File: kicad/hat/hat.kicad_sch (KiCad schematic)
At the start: 6 parts, among them J1 GPIO, J2 FrontButtons, J3 DisplaySPI, J4 DisplayOnOff, J5 PowerButton, J6 PowerWakeup

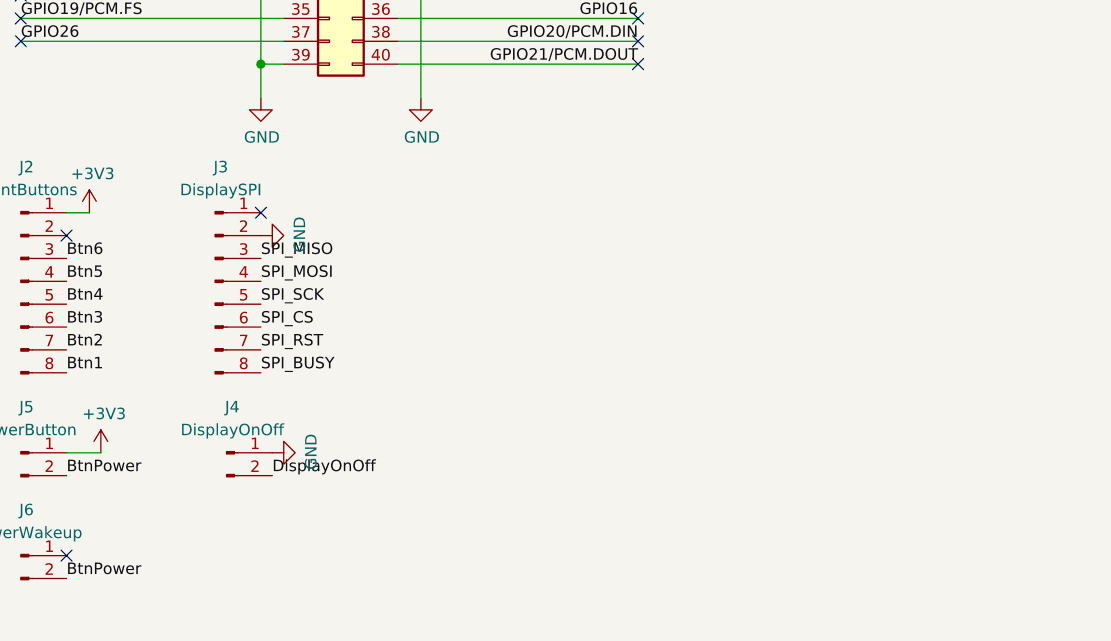
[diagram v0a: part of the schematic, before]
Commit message: addd display on off switch to hat
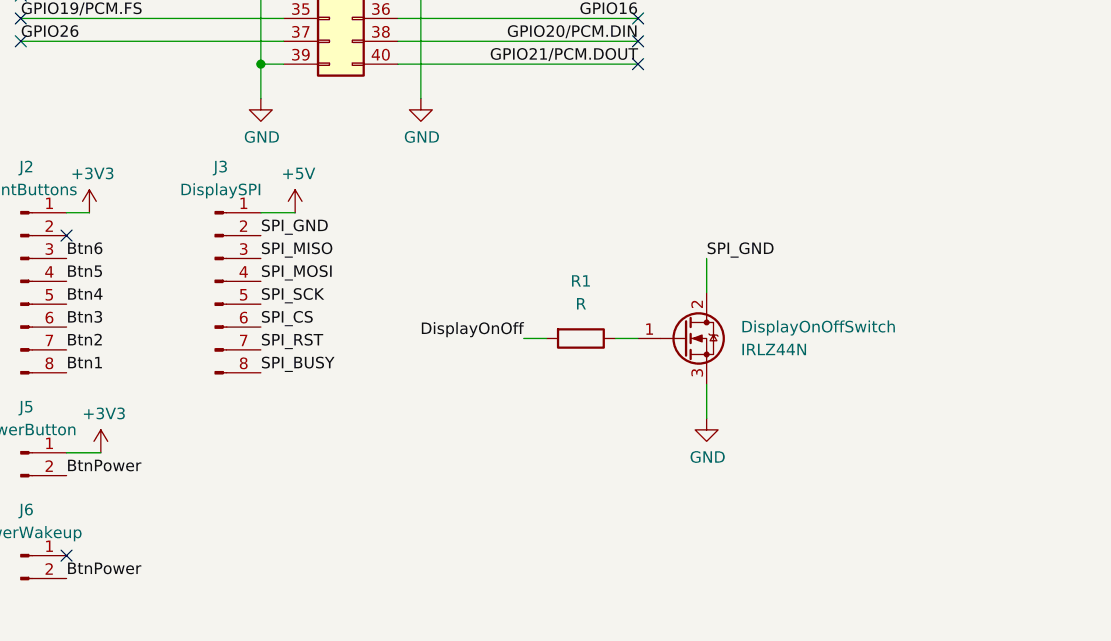
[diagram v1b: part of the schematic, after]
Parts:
- removed J4: DisplayOnOff, symbol Connector:Conn_01x02_Pin
- added DisplayOnOffSwitch: IRLZ44N, Package_TO_SOT_THT:TO-220-3_Vertical, symbol Transistor_FET:IRLZ44N
- added R1: R, symbol Device:R
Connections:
- net +5V: now also J3.1 (Pin_1)
- net DisplayOnOff: now also R1.2
- net GND: now also DisplayOnOffSwitch.3 (S); no longer J3.2 (Pin_2)
- new net: DisplayOnOffSwitch.1 (G), R1.1
- new net SPI_GND: DisplayOnOffSwitch.2 (D), J3.2 (Pin_2)
- no-connect marks 17 -> 16

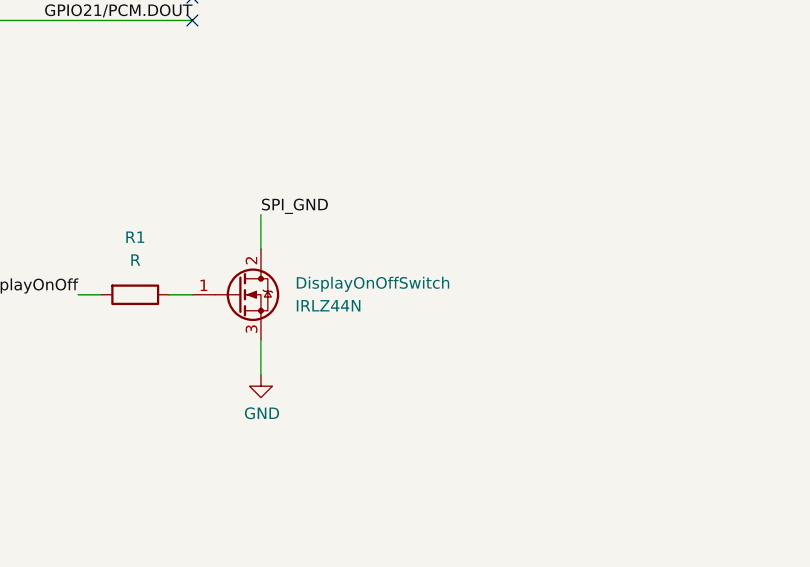
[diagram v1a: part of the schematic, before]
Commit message: add footprints to hat
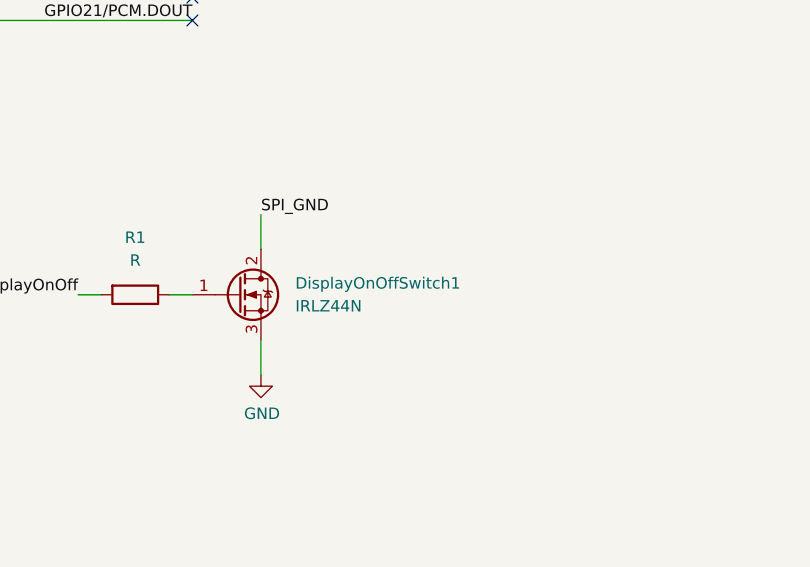
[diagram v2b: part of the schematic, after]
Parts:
- J2, J3: footprint (none) -> Connector_PinHeader_2.54mm:PinHeader_1x08_P2.54mm_Vertical
- J5, J6: footprint (none) -> Connector_PinHeader_2.54mm:PinHeader_1x02_P2.54mm_Vertical
- R1: footprint (none) -> Resistor_THT:R_Axial_DIN0207_L6.3mm_D2.5mm_P10.16mm_Horizontal
- renumbered DisplayOnOffSwitch to DisplayOnOffSwitch1
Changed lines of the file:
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@@
 			)
 		)
-		(property "Footprint" ""
+		(property "Footprint" "Resistor_THT:R_Axial_DIN0207_L6.3mm_D2.5mm_P10.16mm_Horizontal"
 			(at 105.41 111.252 90)
 			(hide yes)
@@
 			)
 		)
-		(property "Footprint" ""
+		(property "Footprint" "Connector_PinHeader_2.54mm:PinHeader_1x02_P2.54mm_Vertical"
 			(at 43.18 125.73 0)
 			(hide yes)
@@
 			)
 		)
-		(property "Footprint" ""
+		(property "Footprint" "Connector_PinHeader_2.54mm:PinHeader_1x02_P2.54mm_Vertical"
 			(at 43.18 137.16 0)
 			(hide yes)
@@
 		(dnp no)
 		(fields_autoplaced yes)
-		(property "Reference" "DisplayOnOffSwitch"
+		(property "Reference" "DisplayOnOffSwitch1"
 			(at 123.19 111.7599 0)
 			(show_name no)
@@
 			(project "hat"
 				(path "/e63e39d7-6ac0-4ffd-8aa3-1841a4541b55"
-					(reference "DisplayOnOffSwitch")
+					(reference "DisplayOnOffSwitch1")
 					(unit 1)
 				)
@@
 			)
 		)
-		(property "Footprint" ""
+		(property "Footprint" "Connector_PinHeader_2.54mm:PinHeader_1x08_P2.54mm_Vertical"
 			(at 64.77 106.68 0)
 			(hide yes)
@@
 			)
 		)
-		(property "Footprint" ""
+		(property "Footprint" "Connector_PinHeader_2.54mm:PinHeader_1x08_P2.54mm_Vertical"
 			(at 43.18 106.68 0)
 			(hide yes)

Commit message: start buttons board
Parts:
- added J7: BatteryLevel, Connector_PinHeader_2.54mm:PinHeader_1x02_P2.54mm_Vertical, symbol Connector:Conn_01x02_Pin
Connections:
- new net PowerboostBat: J7.1 (Pin_1)
- no-connect marks 16 -> 17
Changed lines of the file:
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@@
+	)
+	(no_connect
+		(at 48.26 151.13)
 	)
 	(no_connect
@@
 	(label "GPIO4{slash}GPCLK0"
 		(at 43.18 41.91 0)
+		(effects
+			(font
+				(size 1.27 1.27)
+			)
+			(justify left bottom)
+		)
+	)
+	(label "PowerboostBat"
+		(at 48.26 148.59 0)
 		(effects
 			(font
@@
 					(unit 1)
 				)
+			)
+		)
+	)
+	(symbol
+		(lib_id "Connector:Conn_01x02_Pin")
+		(at 43.18 148.59 0)
+		(unit 1)
+		(body_style 1)
+		(exclude_from_sim no)
+		(in_bom yes)
+		(on_board yes)
+		(in_pos_files yes)
+		(dnp no)
+		(fields_autoplaced yes)
+		(property "Reference" "J7"
+			(at 43.815 143.51 0)
+			(show_name no)
+			(do_not_autoplace no)
+			(effects
+				(font
+					(size 1.27 1.27)
+				)
+			)
+		)
+		(property "Value" "BatteryLevel"
+			(at 43.815 146.05 0)
+			(show_name no)
+			(do_not_autoplace no)
+			(effects
+				(font
+					(size 1.27 1.27)
+				)
+			)
+		)
+		(property "Footprint" "Connector_PinHeader_2.54mm:PinHeader_1x02_P2.54mm_Vertical"
+			(at 43.18 148.59 0)
+			(hide yes)
+			(show_name no)
+			(do_not_autoplace no)
+			(effects
+				(font
+					(size 1.27 1.27)
+				)
+			)
+		)
+		(property "Datasheet" ""
+			(at 43.18 148.59 0)
+			(hide yes)
+			(show_name no)
+			(do_not_autoplace no)
+			(effects
+				(font
+					(size 1.27 1.27)
+				)
+			)
+		)
+		(property "Description" "Generic connector, single row, 01x02, script generated"
+			(at 43.18 148.59 0)
+			(hide yes)
+			(show_name no)
+			(do_not_autoplace no)
+			(effects
+				(font
+					(size 1.27 1.27)
+				)
+			)
+		)
+		(pin "2"
+		)
+		(pin "1"
+		)
+		(instances
+			(project "hat"
+				(path "/e63e39d7-6ac0-4ffd-8aa3-1841a4541b55"
+					(reference "J7")
+					(unit 1)
+				)

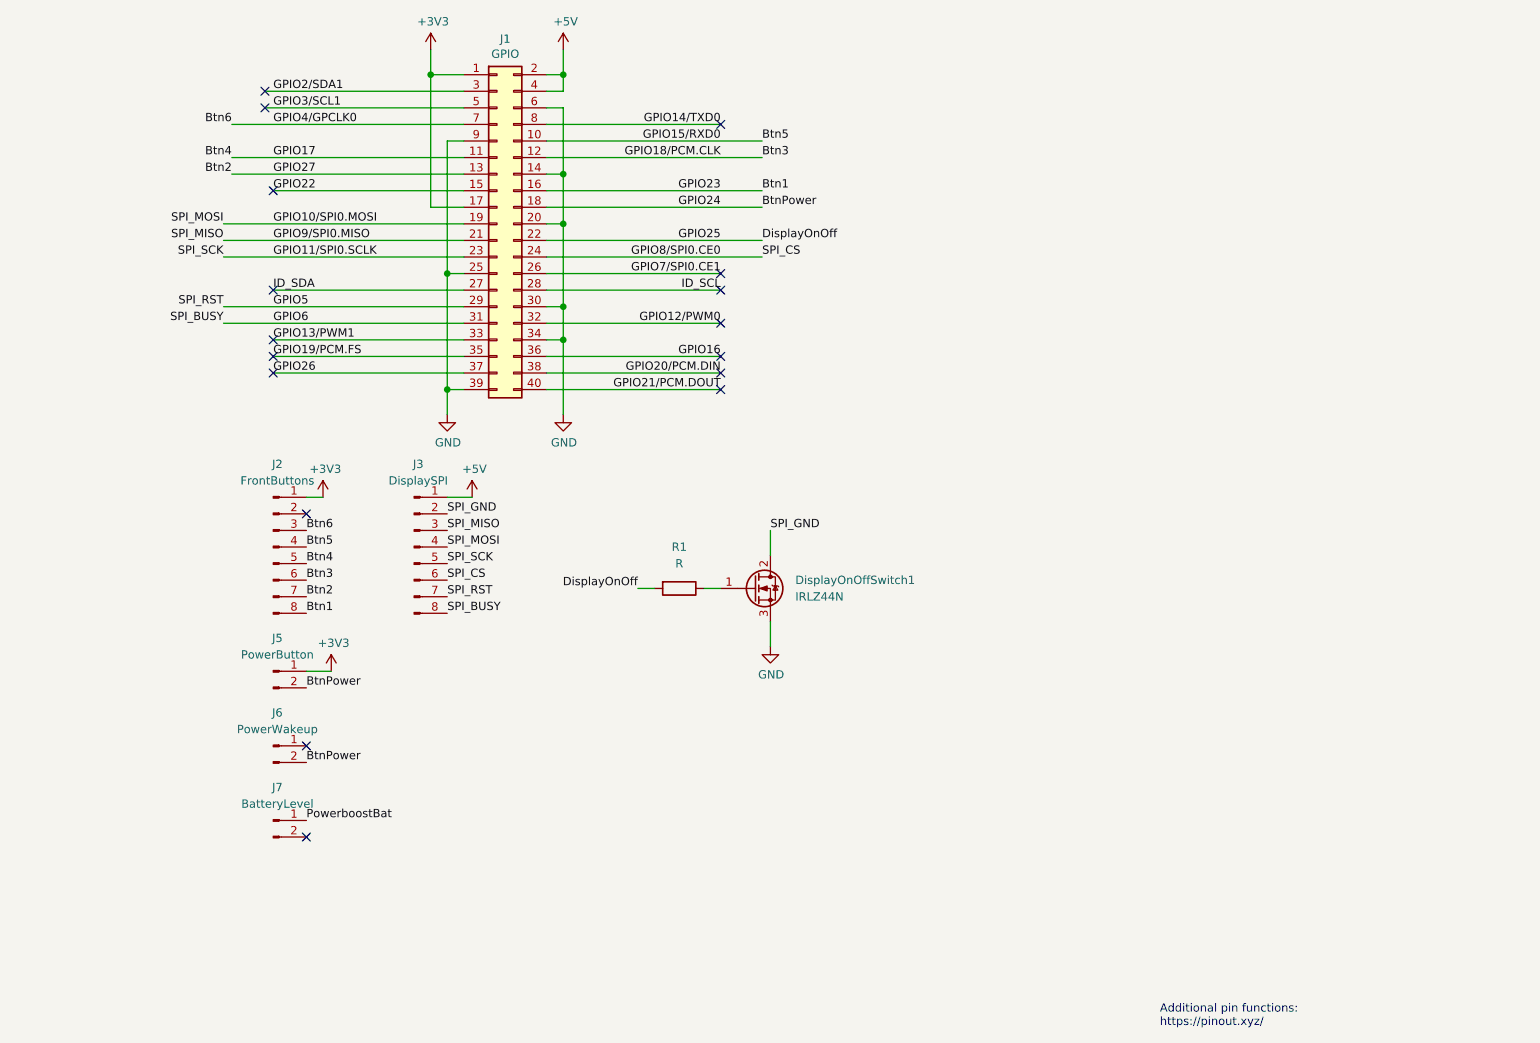
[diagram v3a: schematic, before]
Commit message: connect adc to battery
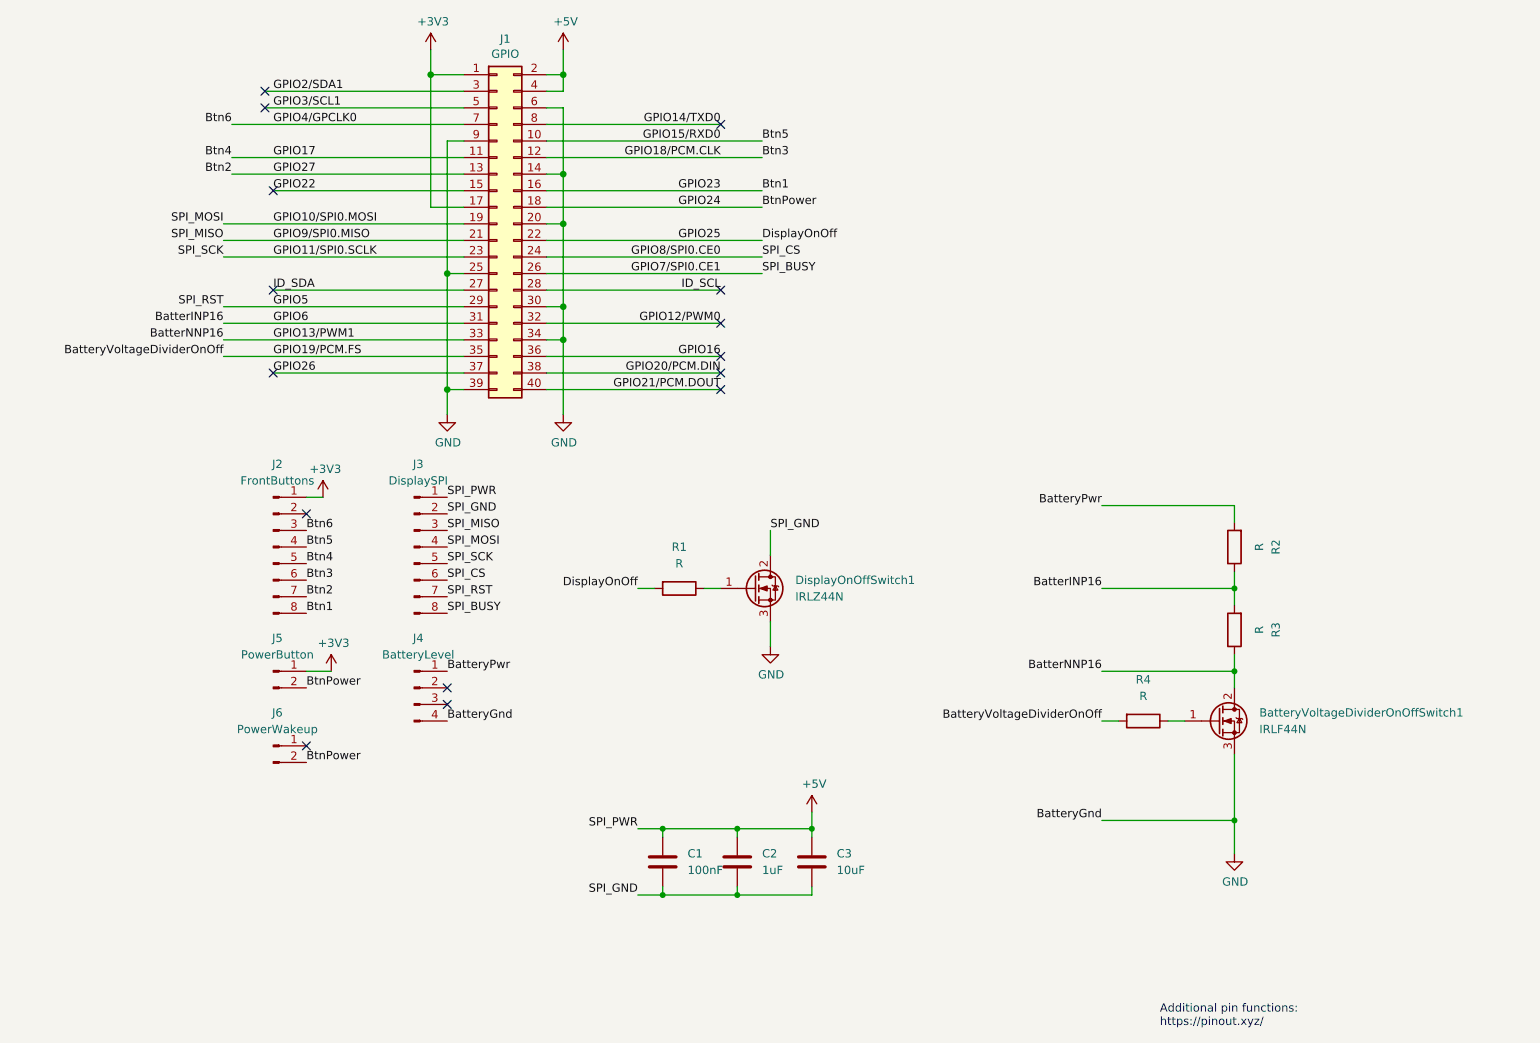
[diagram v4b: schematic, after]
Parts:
- removed J7: BatteryLevel, Connector_PinHeader_2.54mm:PinHeader_1x02_P2.54mm_Vertical, symbol Connector:Conn_01x02_Pin
- added BatteryVoltageDividerOnOffSwitch1: IRLF44N, Package_TO_SOT_THT:TO-220-3_Vertical, symbol Transistor_FET:IRLZ44N
- added C1: 100nF, Capacitor_THT:C_Disc_D10.0mm_W2.5mm_P5.00mm, symbol Device:C
- added C2: 1uF, Capacitor_THT:C_Disc_D10.0mm_W2.5mm_P5.00mm, symbol Device:C
- added C3: 10uF, Capacitor_THT:C_Disc_D10.0mm_W2.5mm_P5.00mm, symbol Device:C
- added J4: BatteryLevel, Connector_PinHeader_2.54mm:PinHeader_1x04_P2.54mm_Vertical, symbol Connector:Conn_01x04_Pin
- added R2, R3, R4: R, Resistor_THT:R_Axial_DIN0207_L6.3mm_D2.5mm_P10.16mm_Horizontal, symbol Device:R
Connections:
- net +5V: now also C1.1, C2.1, C3.1
- net GND: now also BatteryVoltageDividerOnOffSwitch1.3 (S), J4.4 (Pin_4)
- net GPIO7/SPI0.CE1: now also J3.8 (Pin_8)
- net SPI_GND: now also C1.2, C2.2, C3.2
- net GPIO13/PWM1 renamed BatterNNP16
- net BatterNNP16: now also BatteryVoltageDividerOnOffSwitch1.2 (D), R3.1
- net GPIO19/PCM.FS renamed BatteryVoltageDividerOnOff
- net BatteryVoltageDividerOnOff: now also R4.2
- net GPIO6 renamed BatterINP16
- net BatterINP16: now also R2.1, R3.2; no longer J3.8 (Pin_8)
- new net: BatteryVoltageDividerOnOffSwitch1.1 (G), R4.1
- new net BatteryPwr: J4.1 (Pin_1), R2.2
- no-connect marks 17 -> 15

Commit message: fix hat bugs
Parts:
- J3: footprint Connector_PinHeader_2.54mm:PinHeader_1x08_P2.54mm_Vertical -> Connector_PinHeader_2.00mm:PinHeader_1x08_P2.00mm_Vertical
- R1, R4: value R -> 10k
- R2: value R -> 47k
- R3: value R -> 33k
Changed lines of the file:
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@@
 			)
 		)
-		(property "Value" "R"
+		(property "Value" "10k"
 			(at 105.41 109.22 90)
 			(show_name no)
@@
 		(fields_autoplaced yes)
 		(property "Reference" "R2"
-			(at 196.85 106.68 90)
-			(show_name no)
-			(do_not_autoplace no)
-			(effects
-				(font
-					(size 1.27 1.27)
-				)
-			)
-		)
-		(property "Value" "R"
-			(at 194.31 106.68 90)
-			(show_name no)
-			(do_not_autoplace no)
-			(effects
-				(font
-					(size 1.27 1.27)
-				)
+			(at 193.04 105.4099 0)
+			(show_name no)
+			(do_not_autoplace no)
+			(effects
+				(font
+					(size 1.27 1.27)
+				)
+				(justify right)
+			)
+		)
+		(property "Value" "47k"
+			(at 193.04 107.9499 0)
+			(show_name no)
+			(do_not_autoplace no)
+			(effects
+				(font
+					(size 1.27 1.27)
+				)
+				(justify right)
 			)
 		)
@@
 		(fields_autoplaced yes)
 		(property "Reference" "R3"
-			(at 196.85 119.38 90)
-			(show_name no)
-			(do_not_autoplace no)
-			(effects
-				(font
-					(size 1.27 1.27)
-				)
-			)
-		)
-		(property "Value" "R"
-			(at 194.31 119.38 90)
-			(show_name no)
-			(do_not_autoplace no)
-			(effects
-				(font
-					(size 1.27 1.27)
-				)
+			(at 193.04 118.1099 0)
+			(show_name no)
+			(do_not_autoplace no)
+			(effects
+				(font
+					(size 1.27 1.27)
+				)
+				(justify right)
+			)
+		)
+		(property "Value" "33k"
+			(at 193.04 120.6499 0)
+			(show_name no)
+			(do_not_autoplace no)
+			(effects
+				(font
+					(size 1.27 1.27)
+				)
+				(justify right)
 			)
 		)
@@
 			)
 		)
-		(property "Footprint" "Connector_PinHeader_2.54mm:PinHeader_1x08_P2.54mm_Vertical"
+		(property "Footprint" "Connector_PinHeader_2.00mm:PinHeader_1x08_P2.00mm_Vertical"
 			(at 64.77 106.68 0)
 			(hide yes)
@@
 		(in_pos_files yes)
 		(dnp no)
-		(fields_autoplaced yes)
 		(property "Reference" "R4"
-			(at 176.53 127 90)
-			(show_name no)
-			(do_not_autoplace no)
-			(effects
-				(font
-					(size 1.27 1.27)
-				)
-			)
-		)
-		(property "Value" "R"
-			(at 176.53 129.54 90)
-			(show_name no)
-			(do_not_autoplace no)
+			(at 176.53 128.778 90)
+			(show_name no)
+			(do_not_autoplace no)
+			(effects
+				(font
+					(size 1.27 1.27)
+				)
+			)
+		)
+		(property "Value" "10k"
+			(at 176.784 130.81 90)
+			(show_name no)
+			(do_not_autoplace no)
